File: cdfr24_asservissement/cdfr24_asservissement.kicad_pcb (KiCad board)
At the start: 2 copper layers, 102 parts, among them J1 Connecteur batterie, J10 Conn_01x05, J11 Conn_01x03, J12 Conn_01x05, J13 Conn_01x03, J14 Conn_ST_STDC14, J15 Free Connecteur, J2 Conn_01x03, J3 Connecteur Programmation, J4 Connecteur Odométrie, J5 Free Connecteur, J6 Connecteur Odométrie, J7 Conn_01x03, J8 Conn_01x02, J9 Conn_01x02, Q1 Q_NMOS_GDS, U1 LM317_SOT-223, U2 LMR16020PDDA, U3 STM32F401RCTx, U4 LSM6DSL, Y1 Crystal_GND24

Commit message: Place PCB components
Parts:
- R11, Rsense1: footprint Resistor_SMD:R_0805_2012Metric_Pad1.20x1.40mm_HandSolder -> Resistor_SMD:R_2512_6332Metric
- moved D2 118.0 mm to (84.8, 43.2), turned to -90 degrees
- moved C13 107.8 mm to (84.9, 68.4)
- moved C14 107.0 mm to (85.0, 74.2), turned to 180 degrees
- moved C20 104.6 mm to (97.4, 53.8), turned to -90 degrees
- moved C21 104.3 mm to (99.5, 53.8), turned to 90 degrees
- moved Y1 103.7 mm to (85.1, 71.3), turned to 90 degrees
- moved Ren3 99.1 mm to (115.2, 104.1)
- moved J2 97.7 mm to (86.9, 77.8)
- moved D1 96.7 mm to (113.8, 40.1)
- moved J14 95.6 mm to (94.0, 90.7)
- moved Rpul2 95.4 mm to (115.2, 99.8)
- moved J15 93.8 mm to (73.3, 43.9)
- moved Roff2 93.7 mm to (115.2, 90.9)
- moved R6 93.4 mm to (84.8, 37.6), turned to 90 degrees
- moved CR2 93.3 mm to (126.0, 96.9)
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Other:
- board outline added: 102.6 x 77.5 mm

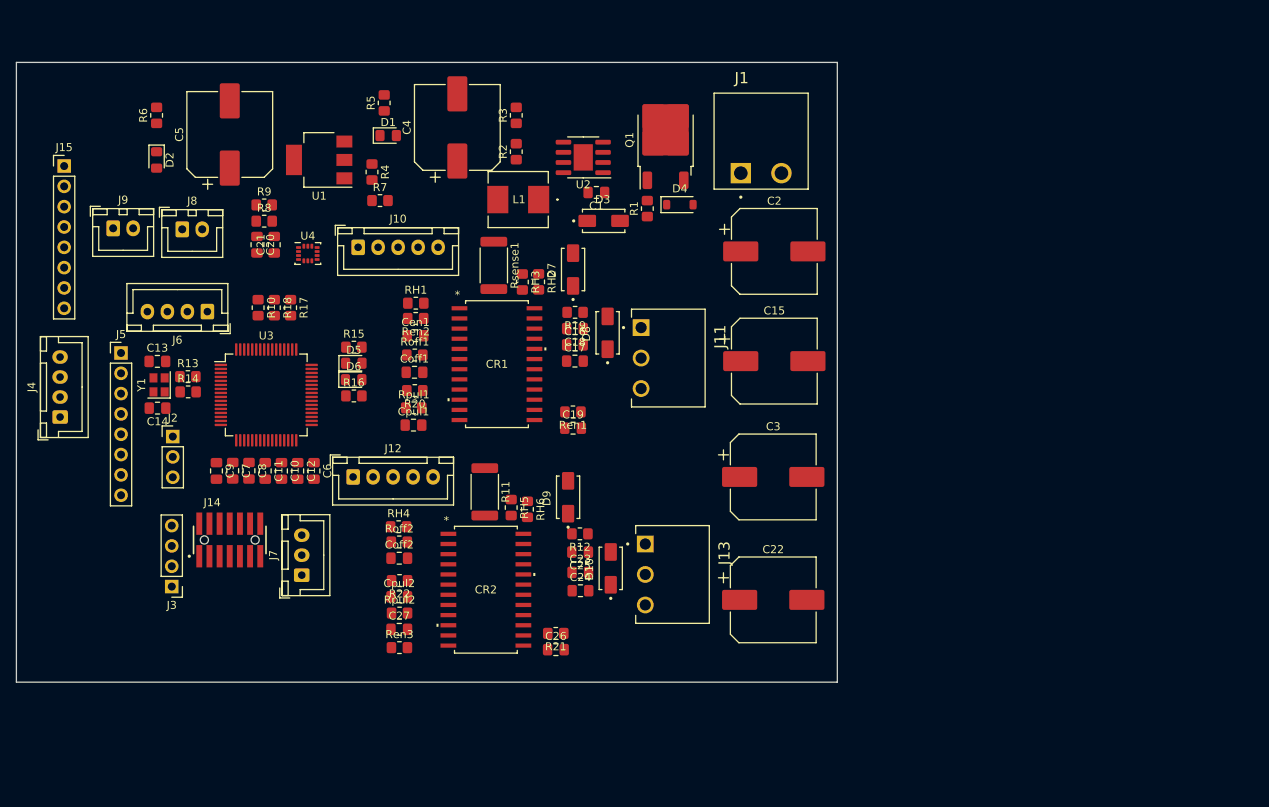
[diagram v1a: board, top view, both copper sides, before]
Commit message: Route PCB, still need to resolve DRC errors
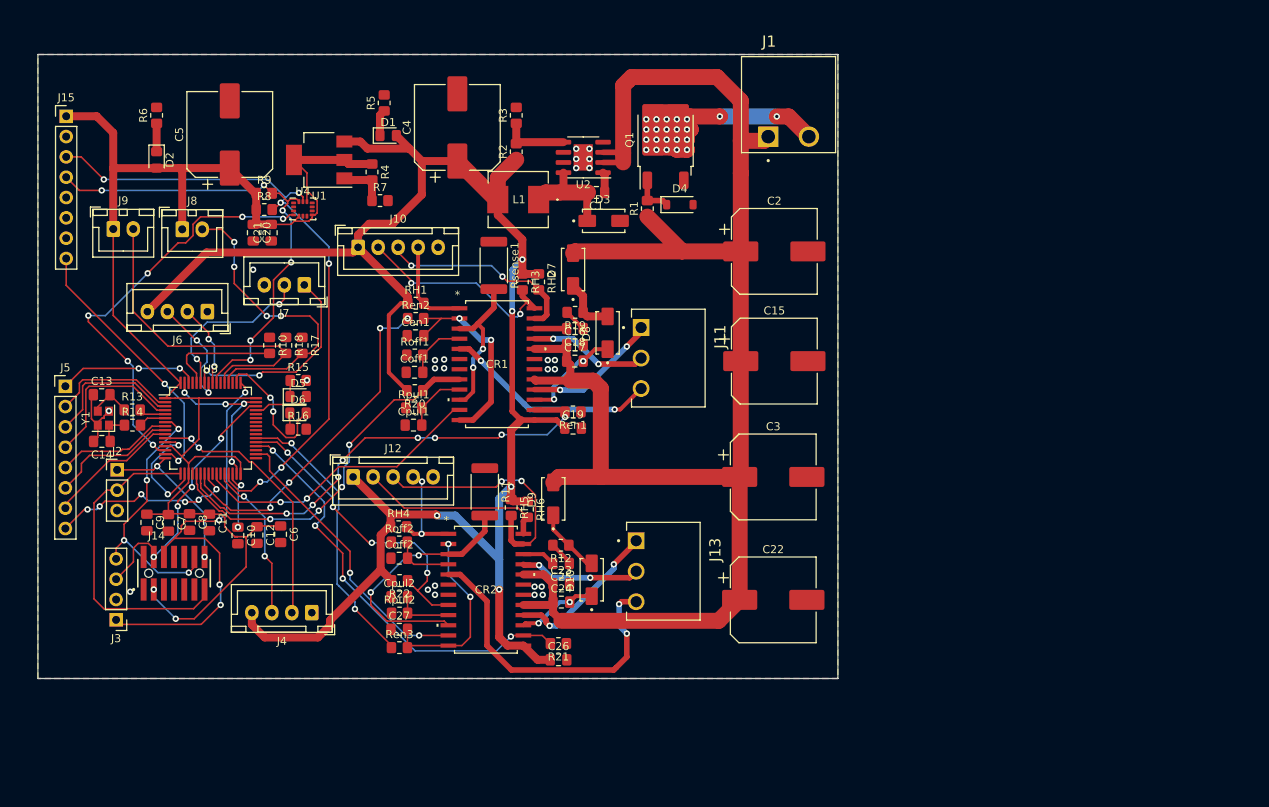
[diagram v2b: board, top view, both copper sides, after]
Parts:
- moved J4 39.9 mm to (104.2, 99.8), turned to 180 degrees
- moved J7 36.3 mm to (103.3, 58.8), turned to 180 degrees
- moved C9 10.8 mm to (83.6, 88.5)
- moved C7 10.3 mm to (86.3, 88.5)
- moved C8 9.81 mm to (89.0, 88.4)
- moved C10 9.74 mm to (95.0, 90.1)
- moved C12 9.49 mm to (97.4, 90.1)
- moved C11 9.49 mm to (91.4, 88.5)
- moved C6 8.95 mm to (100.3, 90.0)
- moved D6 8.11 mm to (102.5, 74.8)
- moved R13 8.11 mm to (81.8, 74.4)
- moved R14 8.11 mm to (81.8, 76.3)
- moved Y1 8.11 mm to (78.2, 75.5)
- moved C13 8.11 mm to (78.0, 72.5)
- moved J14 8.11 mm to (87.0, 94.8)
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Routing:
- net +5V: track 0.00 -> 232.1 mm, vias 0 -> 5
- net +BATT: track 0.00 -> 213.1 mm
- net +3.3V: track 0.00 -> 184.7 mm, vias 0 -> 2
- net /IMU_SCL: track 0.00 -> 82.6 mm, vias 0 -> 6
- net /IMU_SDA: track 0.00 -> 59.7 mm, vias 0 -> 6
- net /BRAKE_L: track 0.00 -> 58.6 mm, vias 0 -> 8
- net SWCLK: track 0.00 -> 55.8 mm, vias 0 -> 4
- net /BRAKE_R: track 0.00 -> 53.8 mm, vias 0 -> 4
- net /IMU_INT1: track 0.00 -> 53.5 mm, vias 0 -> 6
- net /TACHO_L: track 0.00 -> 46.1 mm, vias 0 -> 4
- net GND: track 0.00 -> 43.9 mm, vias 0 -> 31
- net /EN_L: track 0.00 -> 43.2 mm, vias 0 -> 4
- net Net-(J9-Pin_2): track 0.00 -> 41.4 mm
- net /right_driver/OUT1: track 0.00 -> 40.4 mm, vias 0 -> 2
- net /RX: track 0.00 -> 40.3 mm
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- added copper zone on B.Cu, net GND
- added copper zone on F.Cu, net GND
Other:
- board size 102.6 x 77.5 mm -> 100 x 78 mm

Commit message: Resolve some errors
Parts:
- added H1: MountingHole_Pad, MountingHole:MountingHole_3.2mm_M3_Pad_Via, F.Cu at (137.1, 32.5)
- added H2: MountingHole_Pad, MountingHole:MountingHole_3.2mm_M3_Pad_Via, F.Cu at (77.0, 32.5)
- added H3: MountingHole_Pad, MountingHole:MountingHole_3.2mm_M3_Pad_Via, F.Cu at (152.8, 107.5)
- added H4: MountingHole_Pad, MountingHole:MountingHole_3.2mm_M3_Pad_Via, F.Cu at (72.8, 107.0)
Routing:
- net GND: track 43.9 -> 152.6 mm, vias 31 -> 48
- net Net-(J1-Pin_2): track 31.9 -> 33.4 mm
- net +5V: track 232.1 -> 233.1 mm
- net +3.3V: track 184.7 -> 185.2 mm
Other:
- board size 100 x 78 mm -> 102 x 82.8 mm

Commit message: Fixed errors
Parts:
- moved J1 1.76 mm to (161.6, 38.5)
- moved C20 0.33 mm to (96.6, 52.3)
- moved C24 0.30 mm to (135.3, 98.7)
- moved C21 0.16 mm to (99.0, 52.3)
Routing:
- net GND: track 152.6 -> 172.2 mm, vias 48 -> 54
- net +3.3V: track 185.2 -> 191.2 mm
- net Net-(J1-Pin_2): track 33.4 -> 34.5 mm
- net /IMU_SDA: track 60.1 -> 60.9 mm
- net +BATT: track 213.1 -> 213.9 mm
- net /IMU_SCL: track 82.6 -> 83.3 mm
- net /right_driver/H2: track 31.4 -> 32.0 mm
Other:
- board text added: "Calib 1"
- board text added: "Calib 2"
- board text added: "Debug"
- board text added: "Free pins"
- board text added: "I2C"
- board text added: "M_Cap_L"
- board text added: "M_Cap_R"
- board text added: "M_Out_L"
- board text added: "M_Out_R"
- board text added: "Odo 1"
- board text added: "Odo 2"
- board text added: "Out IMU"
- board text added: "Prog"

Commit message: Remove lock
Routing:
- net GND: track 172.2 -> 173.2 mm
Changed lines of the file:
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@@
     (height -13.85)
     (orientation 0)
-    (gr_text "60,0250 mm" (at 107.0375 17.45) (layer "User.1")
+    (gr_text "60.0250 mm" (at 107.0375 17.45) (layer "User.1")
       (effects (font (size 1 1) (thickness 0.15)))
     )
@@
     (height 11.45)
     (orientation 0)
-    (gr_text "80,0000 mm" (at 112.8 117.325) (layer "User.1")
+    (gr_text "80.0000 mm" (at 112.8 117.325) (layer "User.1")
       (effects (font (size 1 1) (thickness 0.15)))
     )
@@
   (segment (start 133.604 68.072) (end 133.731 68.199) (width 0.5) (layer "F.Cu") (net 4))
   (segment (start 138.168 37.682) (end 137.094 36.608) (width 0.7) (layer "F.Cu") (net 4))
+  (segment (start 137.477 42.863) (end 137.287 43.053) (width 0.25) (layer "F.Cu") (net 4))
   (segment (start 114.205 99.822) (end 114.205 97.865) (width 0.25) (layer "F.Cu") (net 4))
   (segment (start 87.0204 96.8756) (end 85.7504 96.8756) (width 0.2) (layer "F.Cu") (net 4))
   (segment (start 116.11 65.203) (end 116.162 65.151) (width 0.5) (layer "F.Cu") (net 4))
+  (segment (start 138.168 42.863) (end 137.477 42.863) (width 0.25) (layer "F.Cu") (net 4))
   (segment (start 132.0673 68.072) (end 133.604 68.072) (width 0.7) (layer "F.Cu") (net 4))
   (segment (start 138.168 42.863) (end 138.168 39.1) (width 0.7) (layer "F.Cu") (net 4))

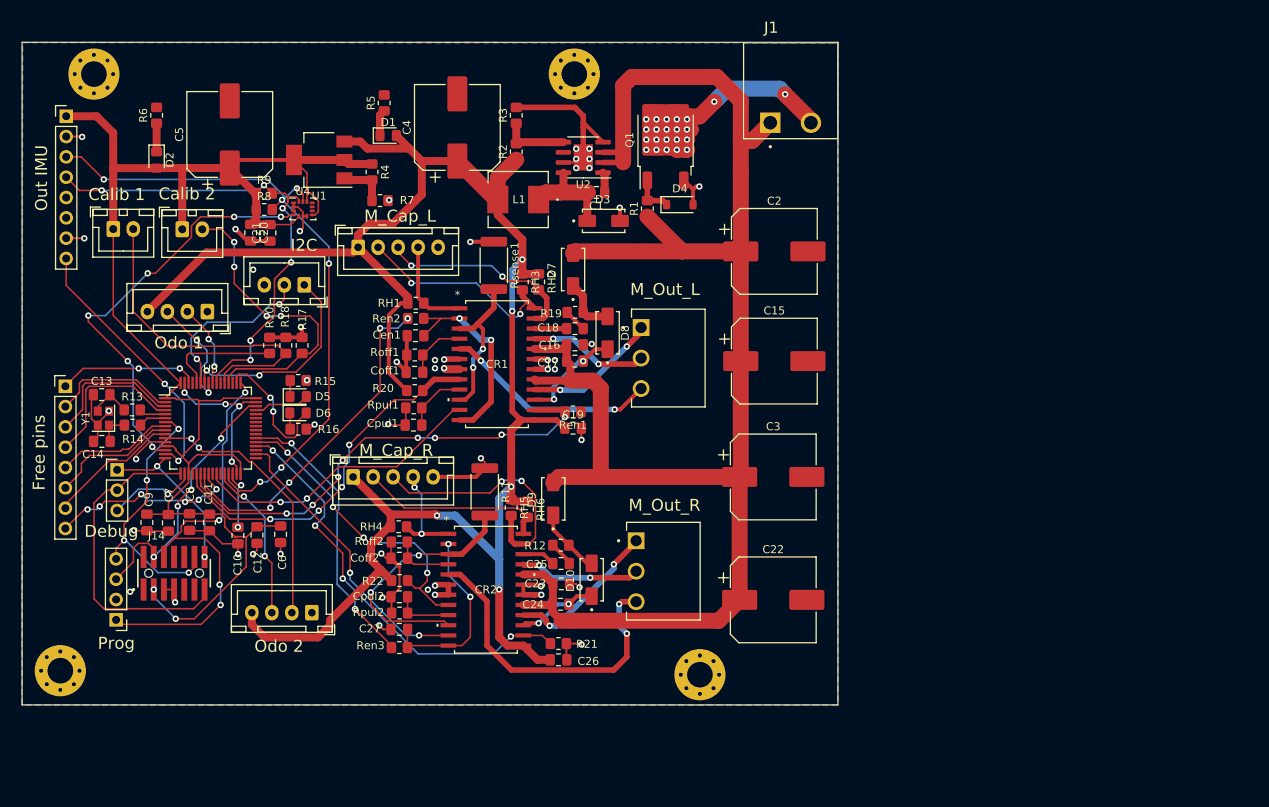
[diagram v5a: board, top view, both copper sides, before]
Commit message: correction Routage
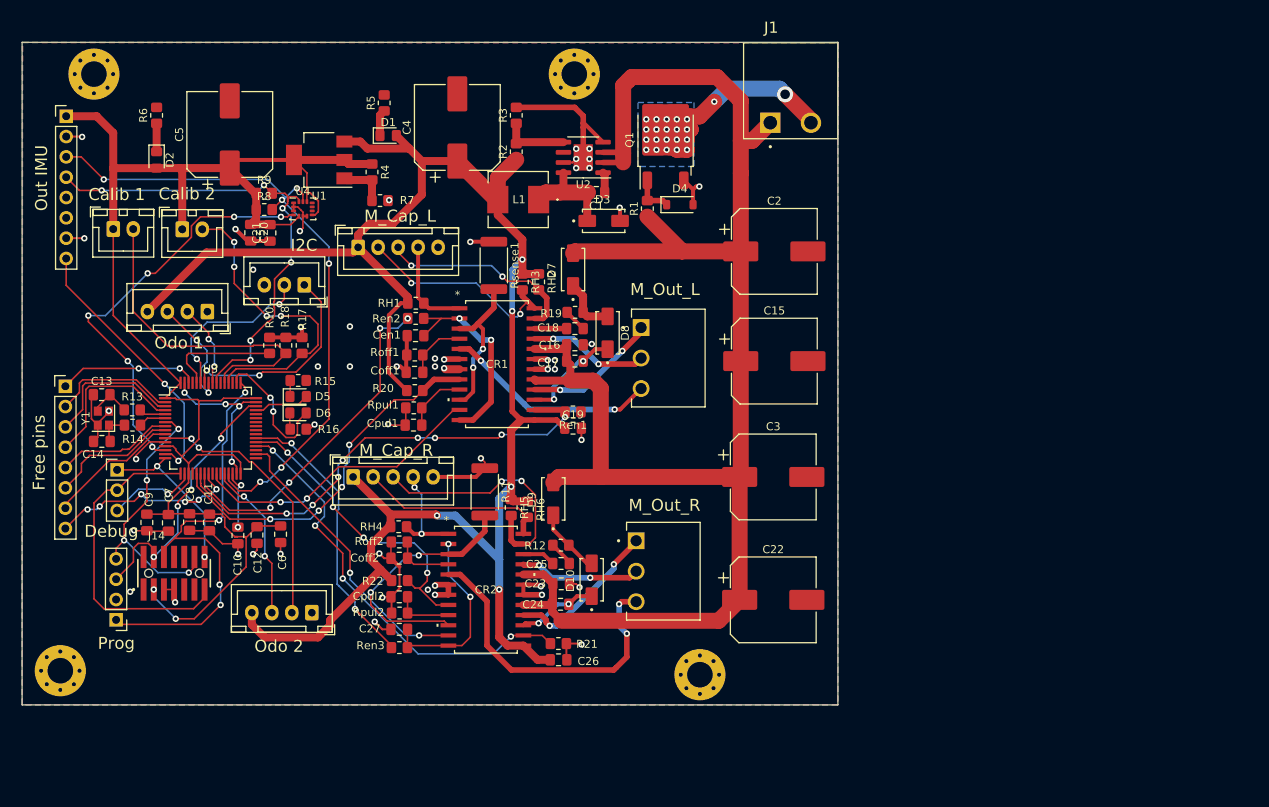
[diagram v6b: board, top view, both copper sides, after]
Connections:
- net Net-(J1-Pin_2) renamed /InputVoltage
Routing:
- net +3.3V: track 191.2 -> 189.4 mm
- net /TX: track 21.4 -> 20.4 mm
- net GND: track 173.2 -> 173.9 mm, vias 54 -> 56
- added copper zone on B.Cu, net /InputVoltage

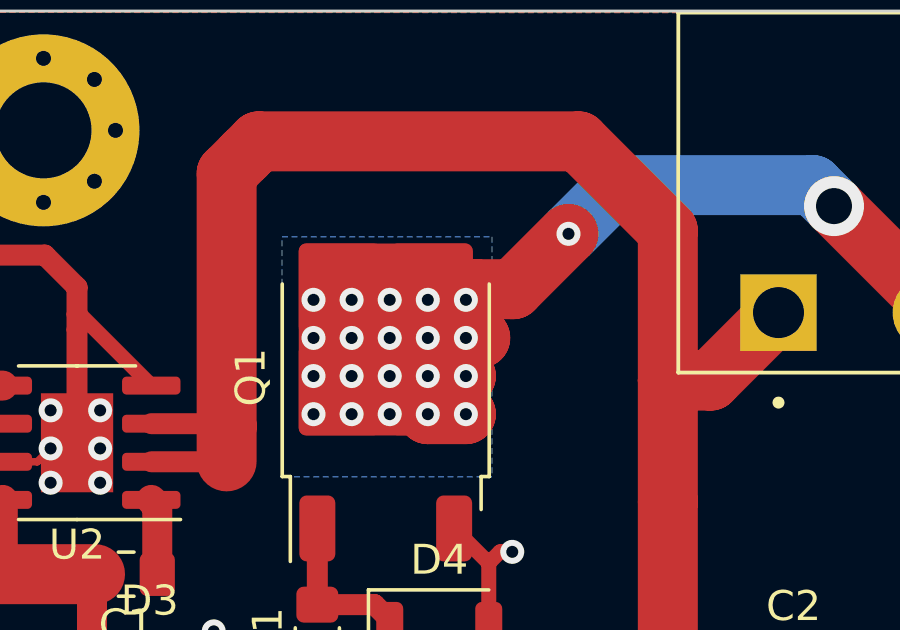
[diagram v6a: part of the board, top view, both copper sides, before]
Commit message: Update via size
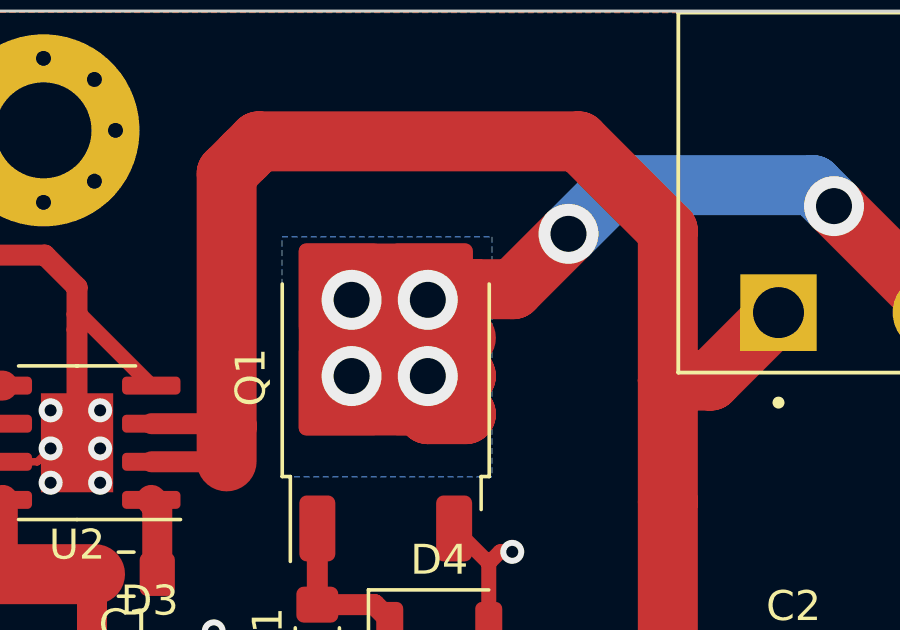
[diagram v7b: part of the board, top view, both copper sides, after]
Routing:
- net /InputVoltage: track 34.5 -> 33.6 mm, vias 22 -> 6
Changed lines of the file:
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@@
     (height -13.85)
     (orientation 0)
-    (gr_text "60,0250 mm" (at 107.0375 17.45) (layer "User.1")
+    (gr_text "60.0250 mm" (at 107.0375 17.45) (layer "User.1")
       (effects (font (size 1 1) (thickness 0.15)))
     )
@@
     (height 11.45)
     (orientation 0)
-    (gr_text "80,0000 mm" (at 112.8 117.325) (layer "User.1")
+    (gr_text "80.0000 mm" (at 112.8 117.325) (layer "User.1")
       (effects (font (size 1 1) (thickness 0.15)))
     )
@@
   (segment (start 149.86 38.1) (end 149.86 37.622) (width 2) (layer "F.Cu") (net 109))
   (segment (start 149.86 39.37) (end 149.86 41.91) (width 2) (layer "F.Cu") (net 109))
-  (segment (start 151.3032 39.0652) (end 151.608 39.37) (width 2) (layer "F.Cu") (net 109))
   (segment (start 149.86 37.622) (end 149.983 37.745) (width 2) (layer "F.Cu") (net 109))
   (segment (start 150.775 37.745) (end 151.13 38.1) (width 2) (layer "F.Cu") (net 109))
@@
   (segment (start 149.983 37.745) (end 150.775 37.745) (width 2) (layer "F.Cu") (net 109))
   (segment (start 151.485 37.745) (end 151.13 38.1) (width 2) (layer "F.Cu") (net 109))
-  (segment (start 151.608 39.37) (end 151.13 39.37) (width 2) (layer "F.Cu") (net 109))
   (segment (start 152.705 37.745) (end 151.485 37.745) (width 2) (layer "F.Cu") (net 109))
-  (via (at 147.32 41.91) (size 0.8) (drill 0.4) (layers "F.Cu" "B.Cu") (net 109))
   (via (at 163.4 34.975) (size 2) (drill 1.2) (layers "F.Cu" "B.Cu") (net 109))
-  (via (at 148.59 41.91) (size 0.8) (drill 0.4) (layers "F.Cu" "B.Cu") (net 109))
-  (via (at 151.13 41.91) (size 0.8) (drill 0.4) (layers "F.Cu" "B.Cu") (net 109))
-  (via (at 148.59 38.1) (size 0.8) (drill 0.4) (layers "F.Cu" "B.Cu") (net 109))
-  (via (at 146.05 38.1) (size 0.8) (drill 0.4) (layers "F.Cu" "B.Cu") (net 109))
-  (via (at 146.05 41.91) (size 0.8) (drill 0.4) (layers "F.Cu" "B.Cu") (net 109))
-  (via (at 146.05 40.64) (size 0.8) (drill 0.4) (layers "F.Cu" "B.Cu") (net 109))
-  (via (at 147.32 40.64) (size 0.8) (drill 0.4) (layers "F.Cu" "B.Cu") (net 109))
-  (via (at 151.13 38.1) (size 0.8) (drill 0.4) (layers "F.Cu" "B.Cu") (net 109))
-  (via (at 149.86 38.1) (size 0.8) (drill 0.4) (layers "F.Cu" "B.Cu") (net 109))
-  (via (at 148.59 40.64) (size 0.8) (drill 0.4) (layers "F.Cu" "B.Cu") (net 109))
-  (via (at 151.13 40.64) (size 0.8) (drill 0.4) (layers "F.Cu" "B.Cu") (net 109))
-  (via (at 151.13 39.37) (size 0.8) (drill 0.4) (layers "F.Cu" "B.Cu") (net 109))
-  (via (at 154.55 35.9) (size 0.8) (drill 0.4) (layers "F.Cu" "B.Cu") (net 109))
-  (via (at 146.05 39.37) (size 0.8) (drill 0.4) (layers "F.Cu" "B.Cu") (net 109))
-  (via (at 149.86 39.37) (size 0.8) (drill 0.4) (layers "F.Cu" "B.Cu") (net 109))
-  (via (at 149.86 41.91) (size 0.8) (drill 0.4) (layers "F.Cu" "B.Cu") (net 109))
-  (via (at 149.86 40.64) (size 0.8) (drill 0.4) (layers "F.Cu" "B.Cu") (net 109))
-  (via (at 148.59 39.37) (size 0.8) (drill 0.4) (layers "F.Cu" "B.Cu") (net 109))
-  (via (at 147.32 39.37) (size 0.8) (drill 0.4) (layers "F.Cu" "B.Cu") (net 109))
-  (via (at 147.32 38.1) (size 0.8) (drill 0.4) (layers "F.Cu" "B.Cu") (net 109))
+  (via (at 147.32 40.64) (size 2) (drill 1.2) (layers "F.Cu" "B.Cu") (net 109))
+  (via (at 149.86 38.1) (size 2) (drill 1.2) (layers "F.Cu" "B.Cu") (net 109))
+  (via (at 154.55 35.9) (size 2) (drill 1.2) (layers "F.Cu" "B.Cu") (net 109))
+  (via (at 149.86 40.64) (size 2) (drill 1.2) (layers "F.Cu" "B.Cu") (net 109))
+  (via (at 147.32 38.1) (size 2) (drill 1.2) (layers "F.Cu" "B.Cu") (net 109))
   (segment (start 163.4 34.975) (end 162.7 34.275) (width 2) (layer "B.Cu") (net 109))
   (segment (start 162.7 34.275) (end 156.175 34.275) (width 2) (layer "B.Cu") (net 109))
